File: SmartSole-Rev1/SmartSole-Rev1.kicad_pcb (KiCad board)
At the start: 2 copper layers, 9 parts, among them U1 MCP6004

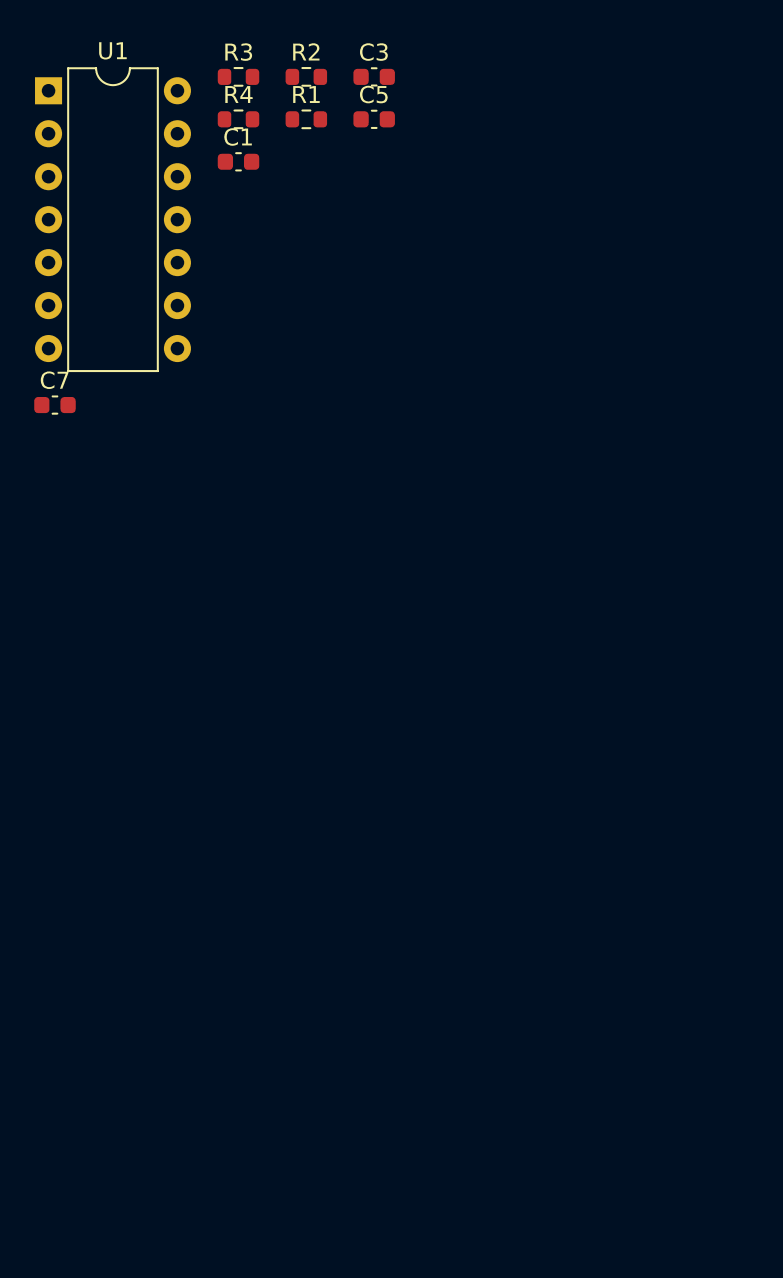
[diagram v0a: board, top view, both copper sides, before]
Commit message: Created prelimary board layout, no finalized traces
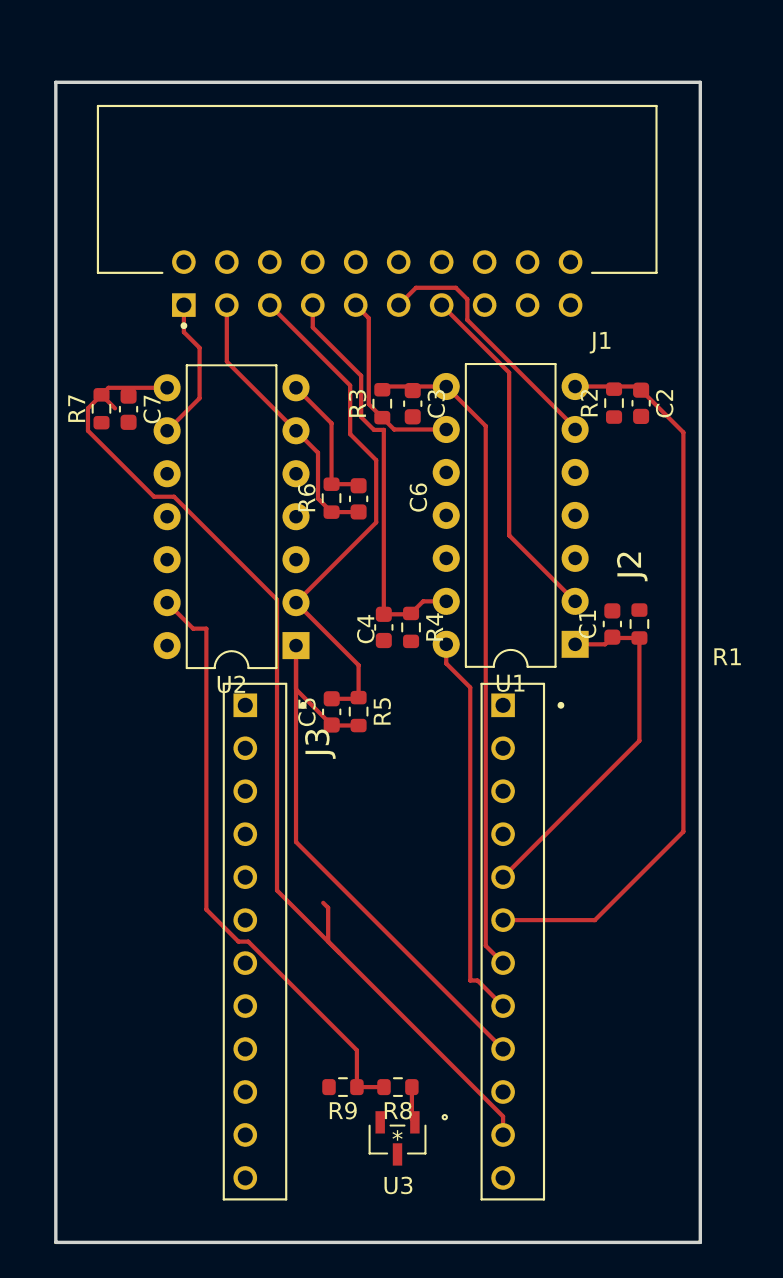
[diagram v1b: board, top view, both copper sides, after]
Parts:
- added C2: 47pF, Capacitor_SMD:C_0603_1608Metric, F.Cu at (150.4, 82.5)
- added C4: 47pF, Capacitor_SMD:C_0603_1608Metric, F.Cu at (135.2, 95.7)
- added C6: 47pF, Capacitor_SMD:C_0603_1608Metric, F.Cu at (133.7, 88.1)
- added J1: 5103310-5, CapstoneLibrary:TE_5103310-5, F.Cu at (134.8, 75.4)
- added J2: 1-825433-2, CapstoneLibrary:TE_1-825433-2, F.Cu at (142.2, 114.3)
- added J3: 1-825433-2, CapstoneLibrary:TE_1-825433-2, F.Cu at (127.0, 114.3)
- added R5: R, Resistor_SMD:R_0603_1608Metric, F.Cu at (133.7, 100.7)
- added R6: R, Resistor_SMD:R_0603_1608Metric, F.Cu at (132.1, 88.1)
- added R7: R, Resistor_SMD:R_0603_1608Metric, F.Cu at (118.5, 82.8)
- added R8: R, Resistor_SMD:R_0603_1608Metric, F.Cu at (136.0, 122.9)
- added R9: R, Resistor_SMD:R_0603_1608Metric, F.Cu at (132.8, 122.9)
- added U2: MCP6004, Package_DIP:DIP-14_W7.62mm, F.Cu at (130.0, 96.8)
- added U3: AD1583, CapstoneLibrary:AD1583ARTZ-Reel7, F.Cu at (136.0, 126.0)
- moved U1 45.2 mm to (146.5, 96.7), turned to 180 degrees
- moved R1 35.7 mm to (150.3, 95.5), turned to -90 degrees
- moved C1 35.1 mm to (148.7, 95.5), turned to 90 degrees
- moved C5 35.1 mm to (132.1, 100.7), turned to 90 degrees
- moved R4 31.7 mm to (136.8, 95.7), turned to -90 degrees
- moved R2 26.5 mm to (148.8, 82.5), turned to 90 degrees
- moved R3 21.1 mm to (135.1, 82.5), turned to 90 degrees
- moved C3 19.5 mm to (136.9, 82.5), turned to -90 degrees
- moved C7 4.36 mm to (120.1, 82.8), turned to -90 degrees
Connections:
- C1 pad 1: Net-(C1-Pad1) -> /AIN2
- C1 pad 2: Net-(C1-Pad2) -> /ForceIn_1
- C3 pad 1: Net-(C3-Pad1) -> /AIN4
- C3 pad 2: Net-(C3-Pad2) -> /ForceIn_3
- C5 pad 1: Net-(C5-Pad1) -> /AIN6
- C5 pad 2: Net-(C5-Pad2) -> /ForceIn_5
- C7 pad 1: Net-(C7-Pad1) -> /AIN1
- C7 pad 2: Net-(C7-Pad2) -> /ForceIn_7
- R1 pad 1: Net-(C3-Pad2) -> /ForceIn_1
- R1 pad 2: Net-(C3-Pad1) -> /AIN2
- R2 pad 1: Net-(C1-Pad2) -> /ForceIn_2
- R2 pad 2: Net-(C1-Pad1) -> /AIN3
- R3 pad 1: Net-(C7-Pad2) -> /ForceIn_3
- R3 pad 2: Net-(C7-Pad1) -> /AIN4
- R4 pad 1: Net-(C5-Pad2) -> /ForceIn_4
- R4 pad 2: Net-(C5-Pad1) -> /AIN5
- U1 pad 1: Net-(C3-Pad1) -> /AIN2
- U1 pad 13: Net-(C5-Pad2) -> /ForceIn_4
- U1 pad 14: Net-(C5-Pad1) -> /AIN5
- U1 pad 2: Net-(C3-Pad2) -> /ForceIn_1
- U1 pad 4: unconnected-(U1-Pad4) -> /3.3V
- U1 pad 6: Net-(C1-Pad2) -> /ForceIn_2
- U1 pad 7: Net-(C1-Pad1) -> /AIN3
- U1 pad 8: Net-(C7-Pad1) -> /AIN4
- U1 pad 9: Net-(C7-Pad2) -> /ForceIn_3
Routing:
- net /AIN1: track 0.00 -> 63.5 mm
- net /AIN3: track 0.00 -> 44.0 mm
- net /AIN4: track 0.00 -> 39.3 mm
- net /AIN6: track 0.00 -> 36.1 mm
- net Net-(R9-Pad1): track 0.00 -> 35.7 mm
- net /ForceIn_5: track 0.00 -> 30.9 mm
- net /ForceIn_4: track 0.00 -> 24.4 mm
- net /AIN5: track 0.00 -> 23.0 mm
- net /AIN2: track 0.00 -> 21.5 mm
- net /ForceIn_1: track 0.00 -> 20.8 mm
- net /ForceIn_6: track 0.00 -> 16.4 mm
- net /ForceIn_2: track 0.00 -> 15.1 mm
- net /ForceIn_3: track 0.00 -> 11.4 mm
- net /ForceIn_7: track 0.00 -> 8.61 mm
- net /AIN7: track 0.00 -> 8.21 mm
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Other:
- board outline added: 38.1 x 68.6 mm

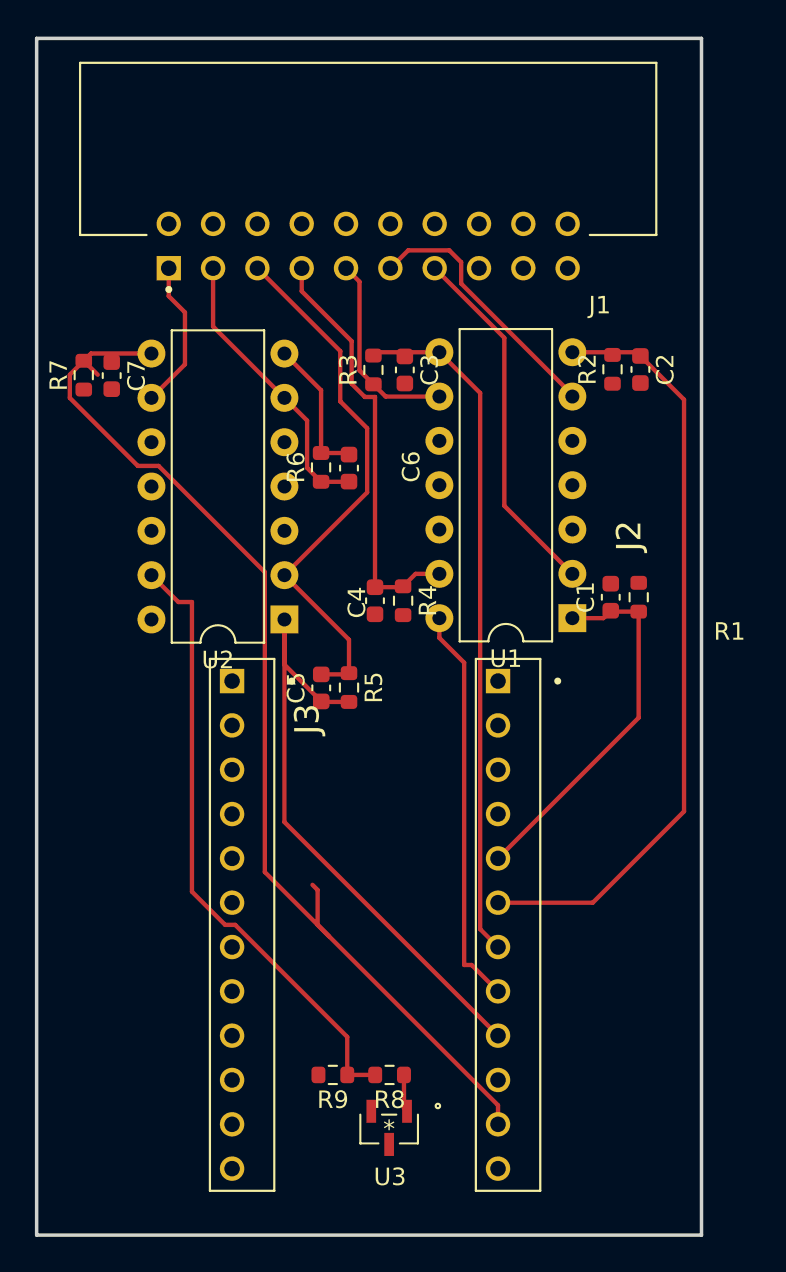
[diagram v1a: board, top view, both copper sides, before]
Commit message: Set positions for Op Amps and resistors in layout
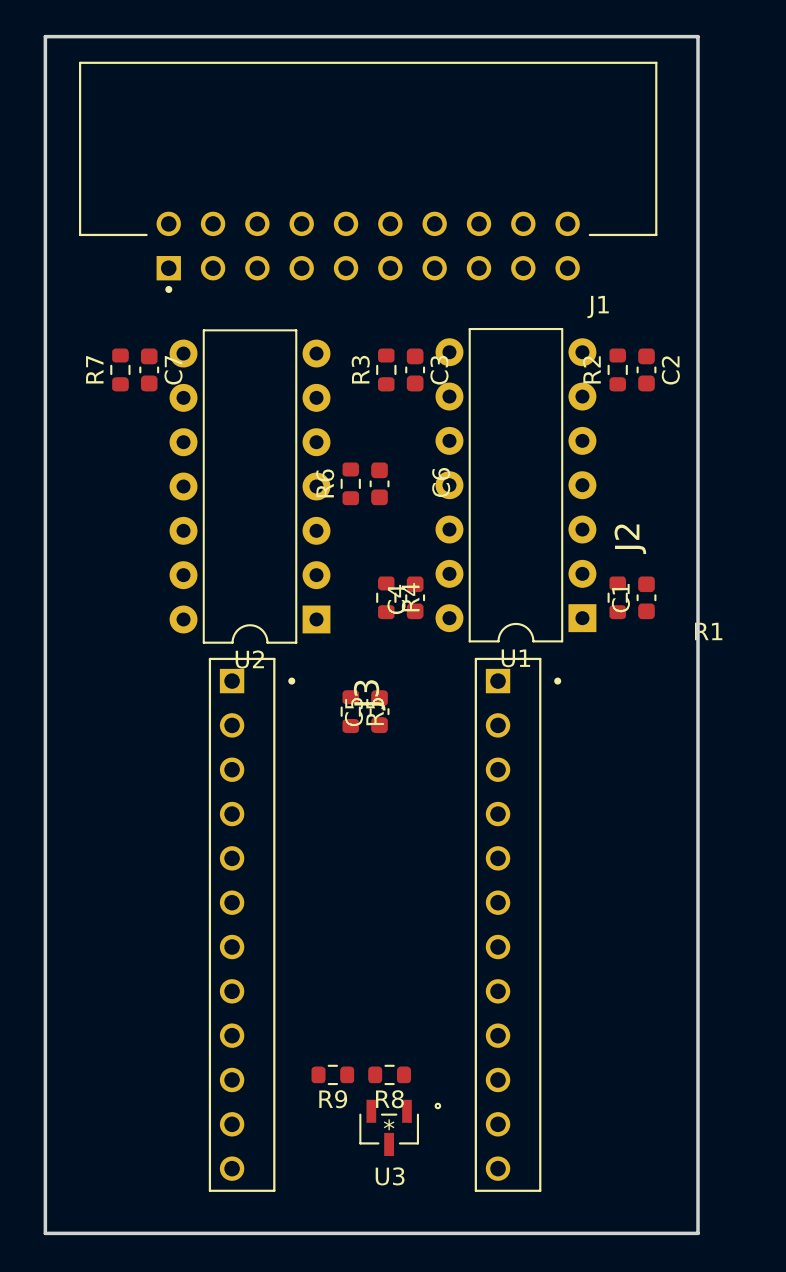
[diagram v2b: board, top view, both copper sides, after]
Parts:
- moved C5 3.61 mm to (135.5, 102.1)
- moved C4 2.31 mm to (137.5, 95.6)
- moved C7 2.18 mm to (122.3, 82.5)
- moved R7 2.12 mm to (120.6, 82.5)
- moved C1 2.05 mm to (150.7, 95.6)
- moved C6 1.97 mm to (135.5, 89.0)
- moved R6 1.94 mm to (133.8, 89.0)
- moved U2 1.84 mm to (131.8, 96.8)
- moved R5 1.39 mm to (133.8, 102.1)
- moved R1 1.20 mm to (149.1, 95.6)
- moved R4 0.98 mm to (135.8, 95.6)
- moved R3 0.74 mm to (135.8, 82.5)
- moved C3 0.59 mm to (137.5, 82.5)
- moved U1 0.58 mm to (147.1, 96.7)
- moved C2 0.35 mm to (150.7, 82.5)
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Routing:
- net /AIN1: track 63.5 -> 0.00 mm
- net /AIN3: track 44.0 -> 0.00 mm
- net /AIN4: track 39.3 -> 0.00 mm
- net /AIN6: track 36.1 -> 0.00 mm
- net Net-(R9-Pad1): track 35.7 -> 0.00 mm
- net /ForceIn_5: track 30.9 -> 0.00 mm
- net /ForceIn_4: track 24.4 -> 0.00 mm
- net /AIN5: track 23.0 -> 0.00 mm
- net /AIN2: track 21.5 -> 0.00 mm
- net /ForceIn_1: track 20.8 -> 0.00 mm
- net /ForceIn_6: track 16.4 -> 0.00 mm
- net /ForceIn_2: track 15.1 -> 0.00 mm
- net /ForceIn_3: track 11.4 -> 0.00 mm
- net /ForceIn_7: track 8.61 -> 0.00 mm
- net /AIN7: track 8.21 -> 0.00 mm
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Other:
- board size 38.1 x 68.6 mm -> 37.4 x 68.6 mm

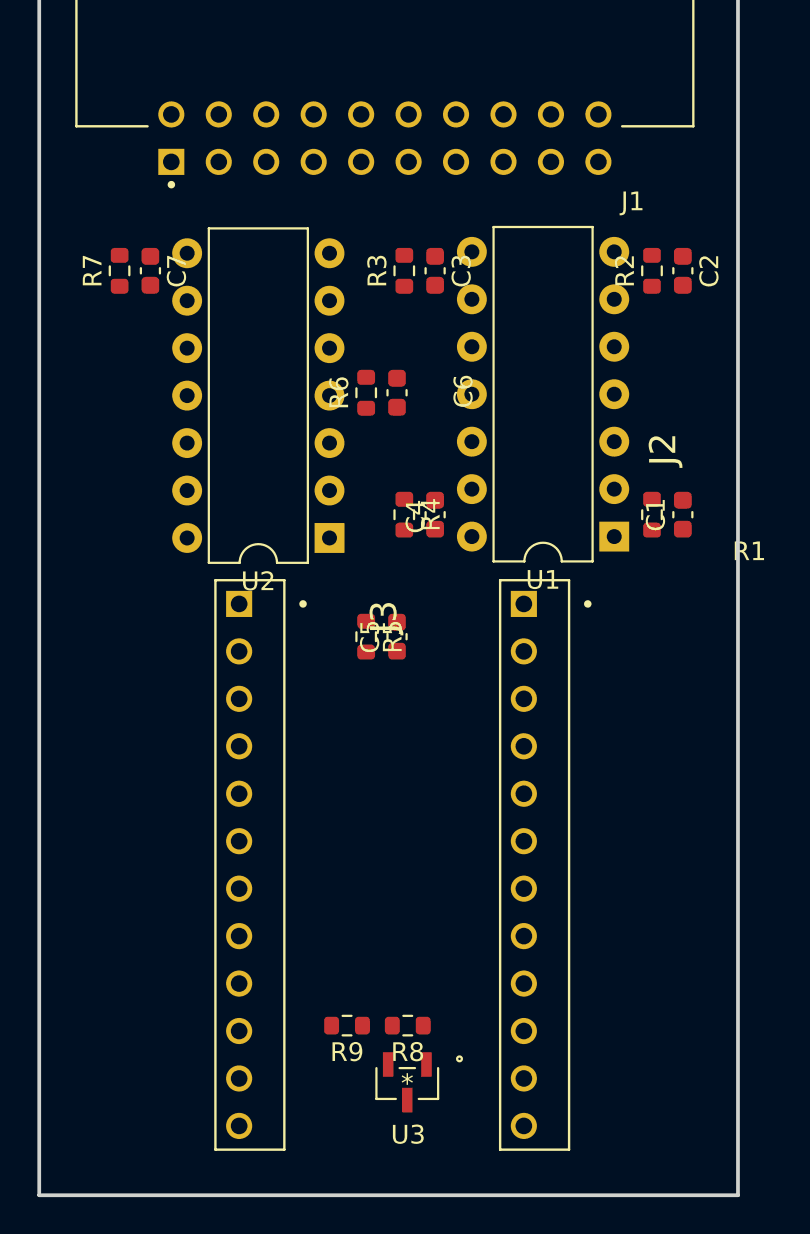
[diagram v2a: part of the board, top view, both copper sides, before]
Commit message: First attempt adding traces to front
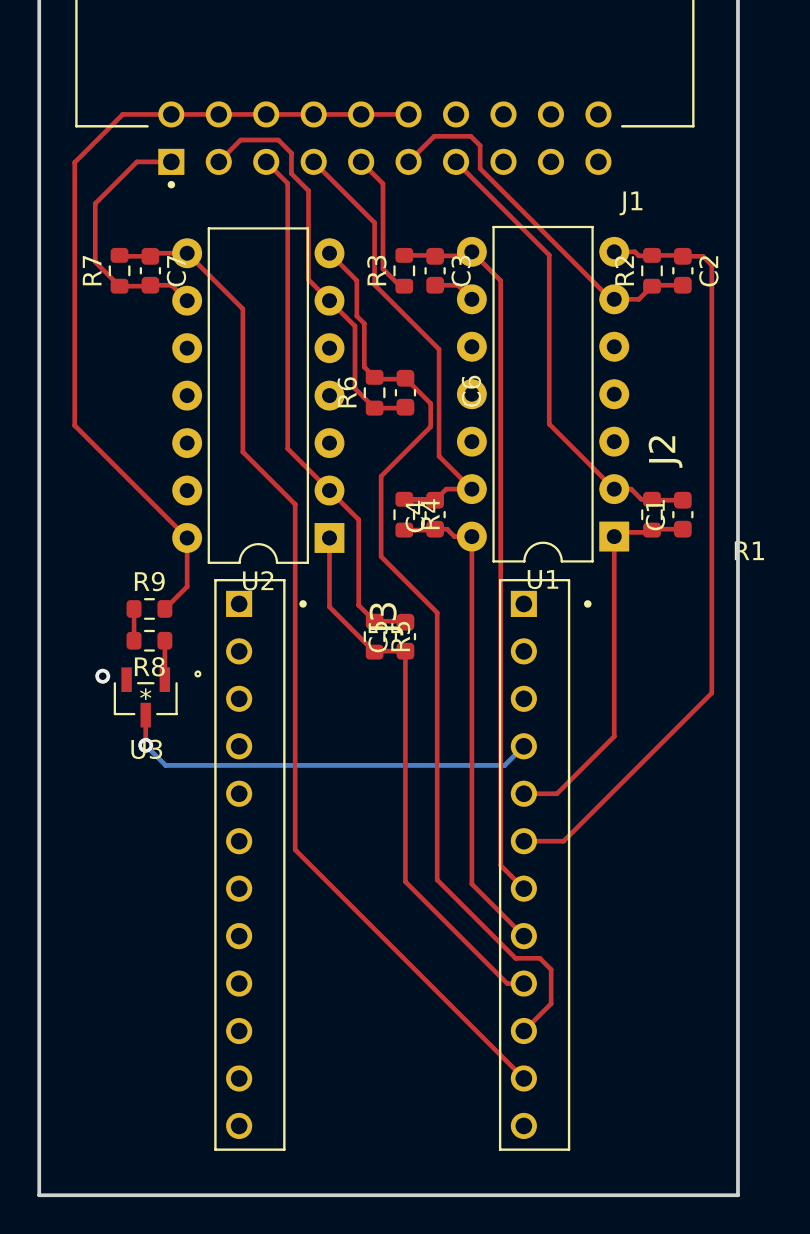
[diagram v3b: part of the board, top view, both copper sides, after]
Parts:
- moved U3 24.9 mm to (122.0, 105.4)
- moved R8 24.8 mm to (122.2, 102.3)
- moved R9 24.7 mm to (122.2, 100.6), turned to 0 degrees
- moved C5 0.45 mm to (135.9, 102.1)
- moved C6 0.45 mm to (135.9, 89.0)
- moved R5 0.45 mm to (134.2, 102.1)
- moved R6 0.45 mm to (134.2, 89.0)
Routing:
- net /AIN1: track 0.00 -> 55.3 mm
- net /AIN7: track 0.00 -> 51.0 mm
- net /VRef: track 0.00 -> 45.8 mm
- net /AIN3: track 0.00 -> 41.8 mm
- net /AIN4: track 0.00 -> 39.0 mm
- net /AIN6: track 0.00 -> 29.7 mm
- net /ForceIn_5: track 0.00 -> 28.7 mm
- net /AIN5: track 0.00 -> 26.9 mm
- net /ForceIn_4: track 0.00 -> 26.6 mm
- net /ForceIn_1: track 0.00 -> 24.9 mm
- net /3.3V: track 0.00 -> 22.7 mm, vias 0 -> 1
- net /ForceIn_6: track 0.00 -> 21.8 mm
- net /AIN2: track 0.00 -> 20.6 mm
- net /ForceIn_2: track 0.00 -> 19.9 mm
- net /ForceIn_7: track 0.00 -> 13.9 mm
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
